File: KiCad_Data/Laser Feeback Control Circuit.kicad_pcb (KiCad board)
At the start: 2 copper layers, 179.6 x 54.4 mm, 101 parts, among them P1 50k, P2 50k, SW1 SPDT Switch, P/N: 7101SD9AV2BE, SW2 SPDT Switch, P/N: 7101SD9AV2BE, SW3 SPDT Switch, P/N: 7101SD9AV2BE, SW4 SPDT Switch, P/N: 7101SD9AV2BE, SW5 SPDT Switch, P/N: 7101SD9AV2BE, SW6 SPDT Switch, P/N: 7101SD9AV2BE, SW7 SPDT Switch, P/N: 7101SD9AV2BE, T1 Transistor P/N: 2N3906, T2 Transistor P/N: 2N3906, T3 Transistor P/N: 2N3906, T4 Transistor P/N: 2N3906

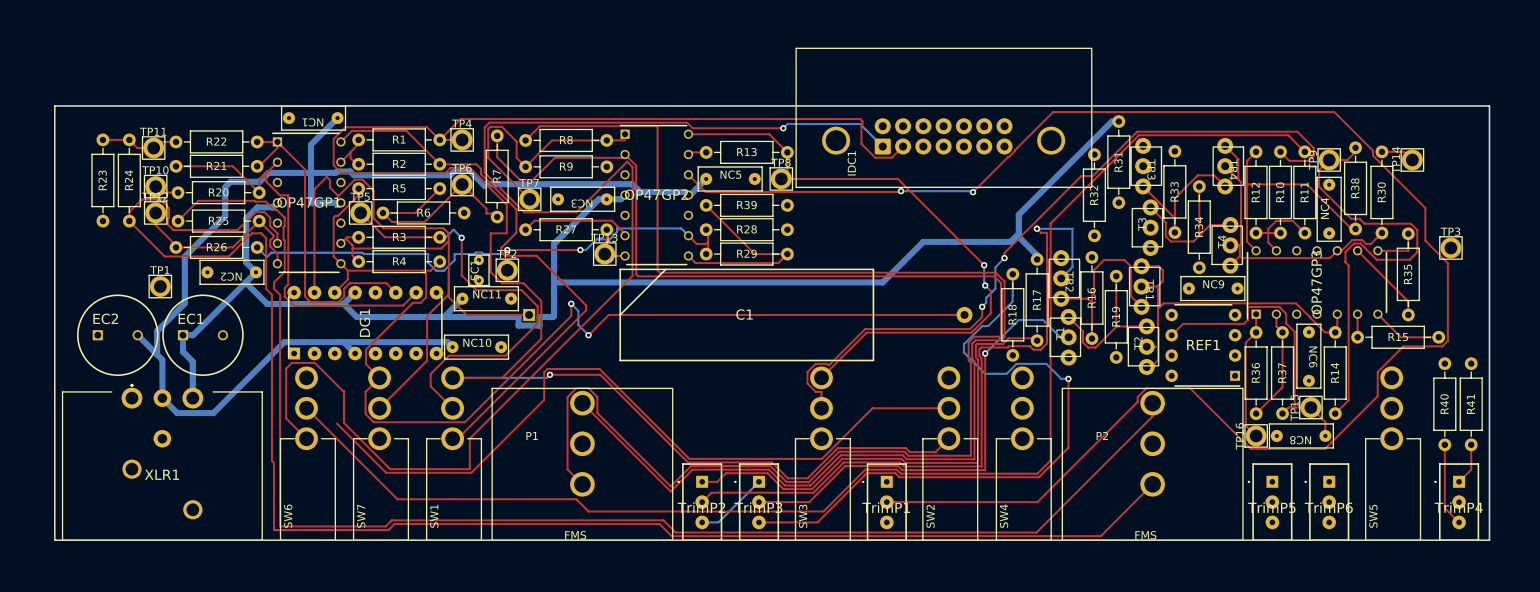
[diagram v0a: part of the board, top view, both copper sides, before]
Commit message: Circuit after correction
Corrections made included: 
- Using quad op-amps which reduced the space needed for the board, however, this made running traces more complicated.
- There was an error with how the IDC connector was set up in this, and all the pins had to be adjusted.
- The circuit that limited the maximum and minimum voltages at the end had a correction added where the previous version had a misconnected trace which caused the whole circuit not to function properly additionally, it was split into 2 separate components which were equivalent but did the opposite action and used to make more sense of the circuit as a whole where each was meant to make the most sense relative to what they were doing (i.e the direction the trim pot was rotated was related to the whether the voltage would decrease or increase).
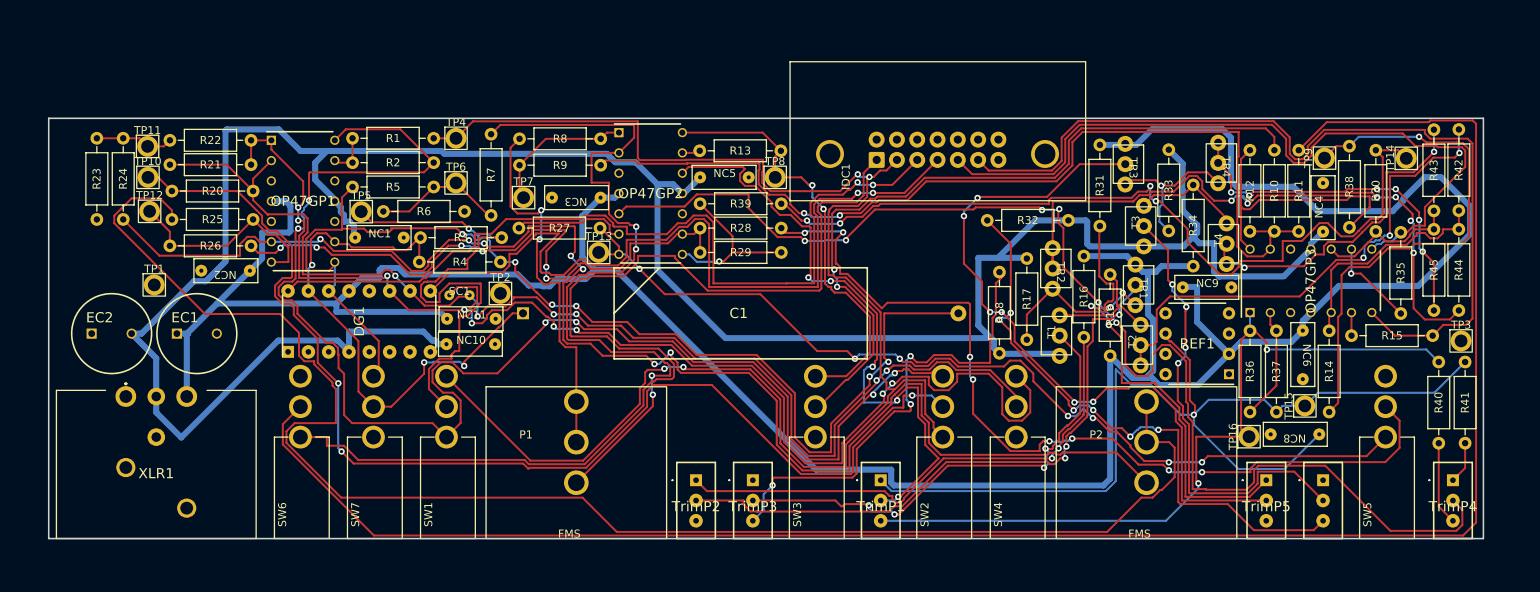
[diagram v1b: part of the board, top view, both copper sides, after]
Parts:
- added R42: 0k, Complex_Op_Amps_Footprints:R_Axial_DIN0207_L6.3mm_D2.5mm_P10.16mm_Horizontal, F.Cu at (206.0, 77.4)
- added R43: 0k, Complex_Op_Amps_Footprints:R_Axial_DIN0207_L6.3mm_D2.5mm_P10.16mm_Horizontal, F.Cu at (202.8, 77.4)
- added R44: 0k, Complex_Op_Amps_Footprints:R_Axial_DIN0207_L6.3mm_D2.5mm_P10.16mm_Horizontal, F.Cu at (206.0, 100.0)
- added R45: 0k, Complex_Op_Amps_Footprints:R_Axial_DIN0207_L6.3mm_D2.5mm_P10.16mm_Horizontal, F.Cu at (202.8, 100.0)
- R16: value 10k -> 5k
- R17: value 5k -> 10k
- SC1: moved to B.Cu
- moved NC1 17.1 mm to (70.9, 90.9), turned to 0 degrees
- moved R32 15.7 mm to (146.9, 88.7), turned to 0 degrees
- moved TP3 11.7 mm to (206.2, 103.8)
- moved R3 7.74 mm to (86.2, 90.9)
- moved R4 7.59 mm to (75.8, 94.0)
- moved SC1 3.96 mm to (80.9, 98.1), turned to 180 degrees
- moved R31 3.76 mm to (161.0, 79.3)
- moved NC11 3.17 mm to (82.4, 101.1)
- moved TP2 3.02 mm to (86.0, 97.9)
- moved TR3 2.25 mm to (164.2, 79.2)
- moved IDC1 1.84 mm to (122.3, 86.3)
- moved R18 1.69 mm to (148.5, 95.2)
- moved TR2 1.64 mm to (155.1, 92.2)
- moved TP10 1.51 mm to (41.9, 83.4)
- moved R17 1.30 mm to (151.9, 93.5)
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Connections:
- R16 pad 1: -15V -> +15V
- R16 pad 2: Net-(TR1-E) -> Net-(R16-Pad2)
- R17 pad 1: +15V -> -15V
- R17 pad 2: Net-(R17-Pad2) -> Net-(TR1-E)
- T2 pad 1: Net-(OP47GP3B-+) -> Net-(T2-B)
- T2 pad 2: Net-(OP47GP3B-+) -> Net-(T2-B)
- T4 pad 1: Net-(OP47GP3C-+) -> Net-(T4-B)
- T4 pad 2: Net-(OP47GP3C-+) -> Net-(T4-B)
- TR1 pad 1: Net-(OP47GP3B-+) -> +15V
- TR1 pad 2: Net-(OP47GP3B-+) -> Net-(TR1-B)
- TR2 pad 1: +15V -> Net-(TR2-B)
- TR4 pad 1: Net-(OP47GP3C-+) -> Net-(TR4-B)
- TR4 pad 2: Net-(OP47GP3C-+) -> Net-(TR4-B)
- TrimP2 pad 1: Net-(R17-Pad2) -> Net-(R16-Pad2)
- TrimP2 pad 2: Net-(TR2-B) -> Net-(TR1-B)
- TrimP2 pad 3: Net-(TrimP2-Pad3) -> GND
- TrimP3 pad 1: Net-(TrimP2-Pad3) -> GND
- TrimP5 pad 3: Net-(TrimP5-Pad3) -> GND
- TrimP6 pad 1: Net-(TrimP5-Pad3) -> GND
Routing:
- net +15V: track 186.2 -> 368.3 mm
- net -15V: track 157.0 -> 315.5 mm
- net Net-(OP47GP2B-+): track 0.00 -> 155.6 mm, vias 0 -> 6
- net Net-(OP47GP2D-+): track 207.7 -> 77.7 mm, vias 2 -> 5
- net Net-(DG1C-S3): track 40.7 -> 162.1 mm, vias 0 -> 9
- net Net-(P1-Pad2): track 162.6 -> 46.9 mm, vias 0 -> 2
- net Net-(SW5-A): track 5.79 -> 117.9 mm, vias 0 -> 7
- net Net-(SW5-B): track 0.00 -> 111.9 mm, vias 0 -> 8
- net Net-(SW1-A): track 70.5 -> 179.4 mm, vias 0 -> 6
- net Net-(DG1B-IN2): track 0.00 -> 107.4 mm, vias 0 -> 2
- net Net-(OP47GP3D--): track 11.8 -> 119.2 mm, vias 0 -> 2
- net Net-(DG1C-IN3): track 0.00 -> 101.7 mm, vias 0 -> 2
- net Net-(IDC1-C-Pad6): track 9.07 -> 109.5 mm
- net Net-(DG1C-D3): track 51.2 -> 150.0 mm, vias 0 -> 6
- net Net-(R30-Pad1): track 4.95 -> 103.7 mm, vias 0 -> 4
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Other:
- board size 179.6 x 54.4 mm -> 179.6 x 52.6 mm
